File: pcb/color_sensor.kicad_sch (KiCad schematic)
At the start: 1 part, among them U3 VEML3328

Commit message: add top level schem and cleanup
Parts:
- renumbered U3 to U4
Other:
- note removed: "10/27/26"
- note removed: "Rev 1"
- note removed: "Topher Fontana"
- note removed: "VEML3328 Schematic"
- title: (none) -> Color Sensor
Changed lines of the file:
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@@
 	(generator_version "10.0")
 	(paper "A4")
-	(text "10/27/26"
-		(exclude_from_sim no)
-		(at 213.36 193.294 0)
-		(effects
-			(font
-				(size 1.27 1.27)
-			)
-		)
-	)
-	(text "VEML3328 Schematic"
-		(exclude_from_sim no)
-		(at 197.866 189.992 0)
-		(effects
-			(font
-				(size 1.27 1.27)
-			)
-		)
-	)
-	(text "Topher Fontana"
-		(exclude_from_sim no)
-		(at 186.182 170.18 0)
-		(effects
-			(font
-				(size 1.27 1.27)
-			)
-		)
-	)
-	(text "Rev 1"
-		(exclude_from_sim no)
-		(at 272.542 193.294 0)
-		(effects
-			(font
-				(size 1.27 1.27)
-			)
-		)
+	(title_block
+		(title "Color Sensor")
+		(date "2026-10-27")
 	)
 	(bus_entry
@@
 		)
 		(instances
+			(project "Onboard_Project"
+				(path "/17df1232-b180-49eb-a49c-63e4861e42e5/b2c0a7fe-fadc-4b67-9c8f-2e9ec056e7a3"
+					(reference "#PWR059")
+					(unit 1)
+				)
+			)
 			(project "Onboadrd_Project"
 				(path "/4ac9cdc8-8624-4651-a962-fae1f7686a01"
@@
 		(dnp no)
 		(fields_autoplaced yes)
-		(property "Reference" "U3"
+		(property "Reference" "U4"
 			(at 128.27 86.36 0)
 			(show_name no)
@@
 		)
 		(instances
+			(project "Onboard_Project"
+				(path "/17df1232-b180-49eb-a49c-63e4861e42e5/b2c0a7fe-fadc-4b67-9c8f-2e9ec056e7a3"
+					(reference "U4")
+					(unit 1)
+				)
+			)
 			(project "Onboadrd_Project"
 				(path "/4ac9cdc8-8624-4651-a962-fae1f7686a01"
@@
 		)
 		(instances
+			(project "Onboard_Project"
+				(path "/17df1232-b180-49eb-a49c-63e4861e42e5/b2c0a7fe-fadc-4b67-9c8f-2e9ec056e7a3"
+					(reference "#PWR058")
+					(unit 1)
+				)
+			)
 			(project "Onboadrd_Project"
 				(path "/4ac9cdc8-8624-4651-a962-fae1f7686a01"
@@
 		)
 	)
-	(sheet_instances
-		(path "/"
-			(page "4")
-		)
-	)

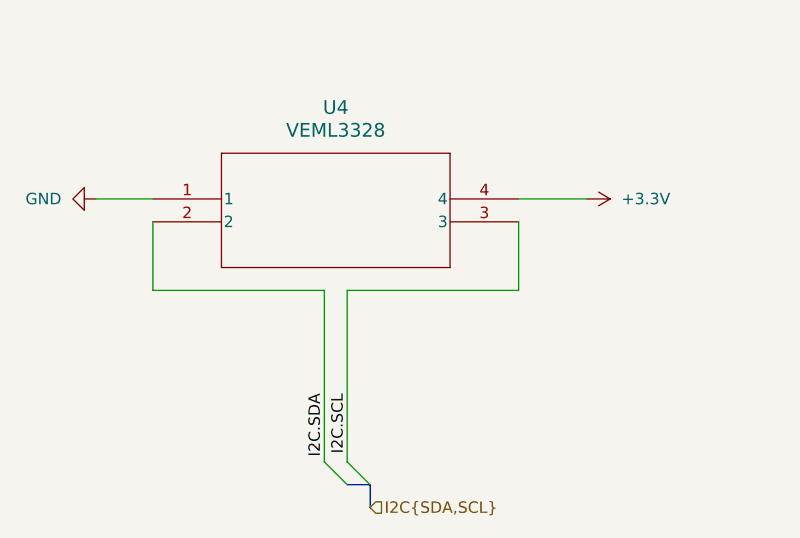
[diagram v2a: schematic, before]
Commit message: custom symbols for all ics
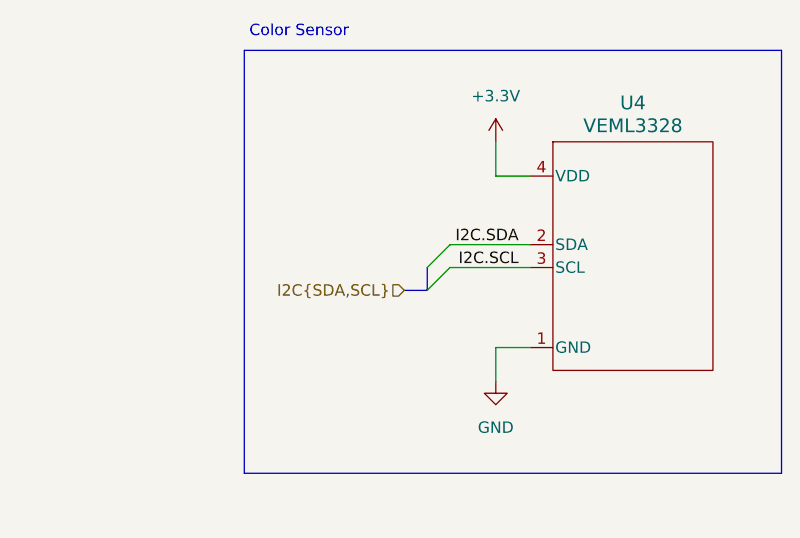
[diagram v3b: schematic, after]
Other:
- note added: "Color Sensor"

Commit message: Slight clean up for HRM
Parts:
- added C24: 0.1u, symbol Device:C
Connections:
- net +3.3V: now also C24.1; no longer U4.4 (VDD)
- net GND: now also C24.2
